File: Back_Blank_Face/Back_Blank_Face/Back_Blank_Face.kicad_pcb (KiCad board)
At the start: 2 copper layers, 87 x 326.5 mm, 10 parts

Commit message: moved holes up 5mm, did what Jack said to do
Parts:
- moved H14 6.55 mm to (172.3, 76.5)
- moved H11 6.52 mm to (96.2, 76.5)
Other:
- outline, holes or cut-outs redrawn

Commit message: changed ALOT of things, got it to a point to send mech models,solar panel harness on BS need changed
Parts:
- added H15: MountingHole, Small_Mounting_Holes:2.0mm_Mounting_Hole, F.Cu at (147.1, -46.2)
- added H16: MountingHole, Small_Mounting_Holes:2.0mm_Mounting_Hole, F.Cu at (147.1, -20.7)
- added H17: MountingHole, Small_Mounting_Holes:2.0mm_Mounting_Hole, F.Cu at (121.6, -20.7)
- added H18: MountingHole, Small_Mounting_Holes:2.0mm_Mounting_Hole, F.Cu at (121.5, -46.2)
- added H19: MountingHole, Small_Mounting_Holes:2.0mm_Mounting_Hole, F.Cu at (166.4, 54.2)
- added H20: MountingHole, Small_Mounting_Holes:2.0mm_Mounting_Hole, F.Cu at (145.2, 54.2)
- added H21: MountingHole, Small_Mounting_Holes:2.0mm_Mounting_Hole, F.Cu at (166.4, 33.0)
- added H22: MountingHole, Small_Mounting_Holes:2.0mm_Mounting_Hole, F.Cu at (145.2, 33.0)
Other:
- outline, holes or cut-outs redrawn

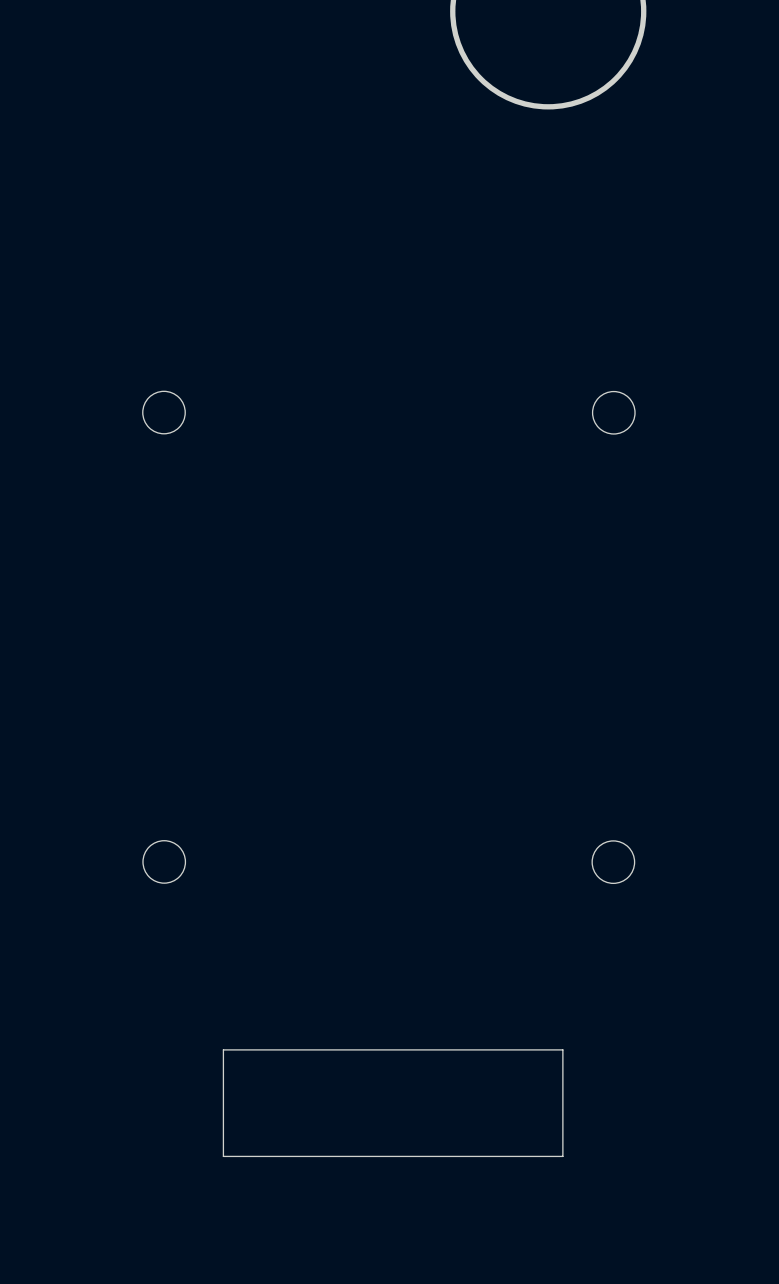
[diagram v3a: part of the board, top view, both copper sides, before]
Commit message: Removed GND and PWR plane, replaced with traces, switches are now in series rather than in parallel
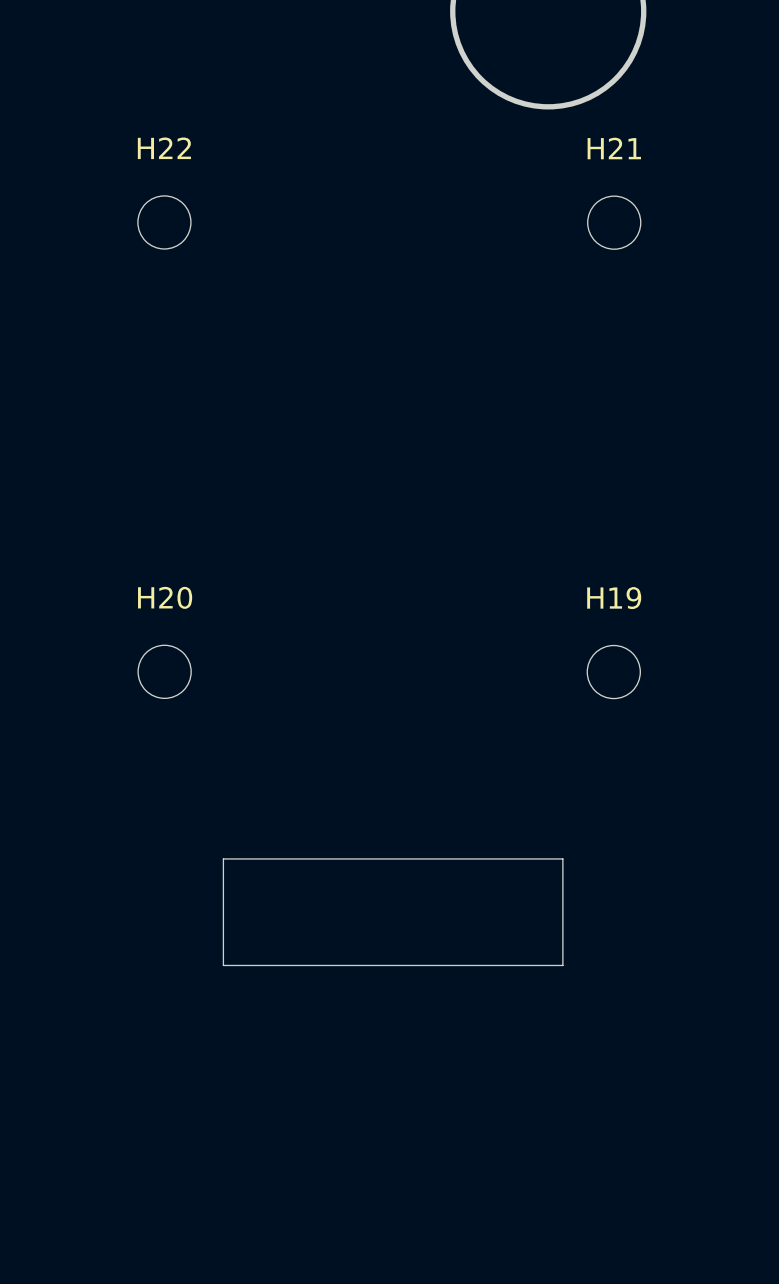
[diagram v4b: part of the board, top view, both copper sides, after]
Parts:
- H19, H20, H21, H22: footprint Small_Mounting_Holes:2.0mm_Mounting_Hole -> MountingHole:MountingHole_2.5mm
- moved H21 9.00 mm to (166.4, 24.0)
- moved H19 9.00 mm to (166.4, 45.2)
- moved H20 9.00 mm to (145.2, 45.2)
- moved H22 9.00 mm to (145.2, 24.0)
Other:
- outline, holes or cut-outs redrawn

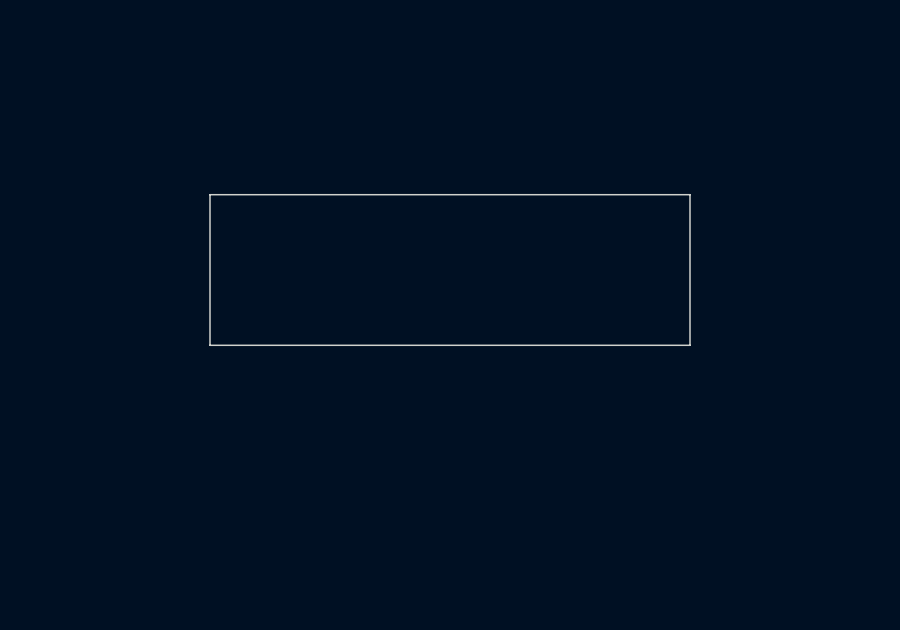
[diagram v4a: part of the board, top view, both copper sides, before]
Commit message: changed cover panels to have smaller power planes, also changed front panel DF13 from SMD to THT
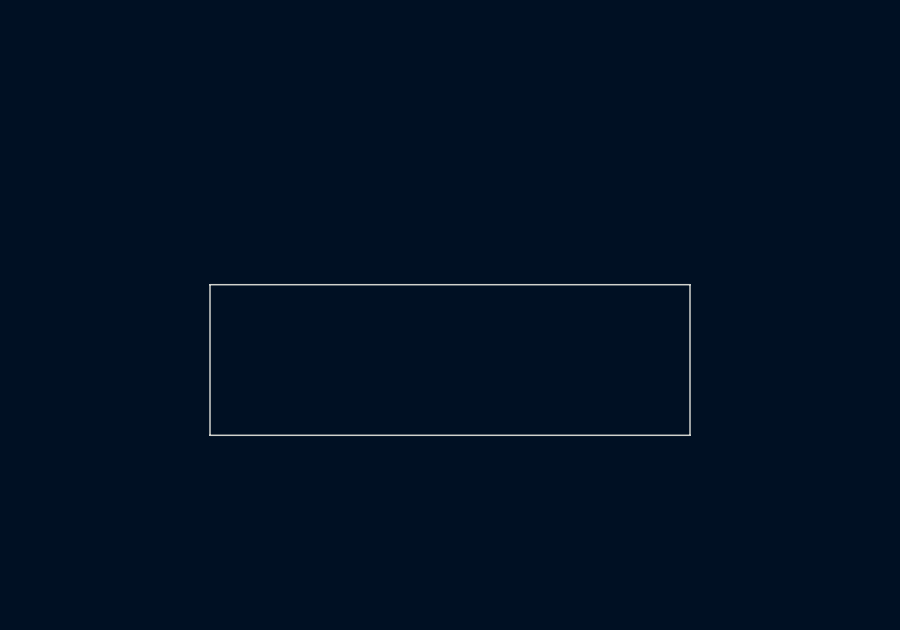
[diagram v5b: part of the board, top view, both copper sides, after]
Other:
- outline, holes or cut-outs redrawn
